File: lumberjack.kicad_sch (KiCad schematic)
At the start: 159 parts, among them J1 USB, J2 AVR_ISP_6, J3 JST, J4 JST, SW1 RESET, SW2 BOOT, U1 ATMEGA328-PU, Y1 16MHz

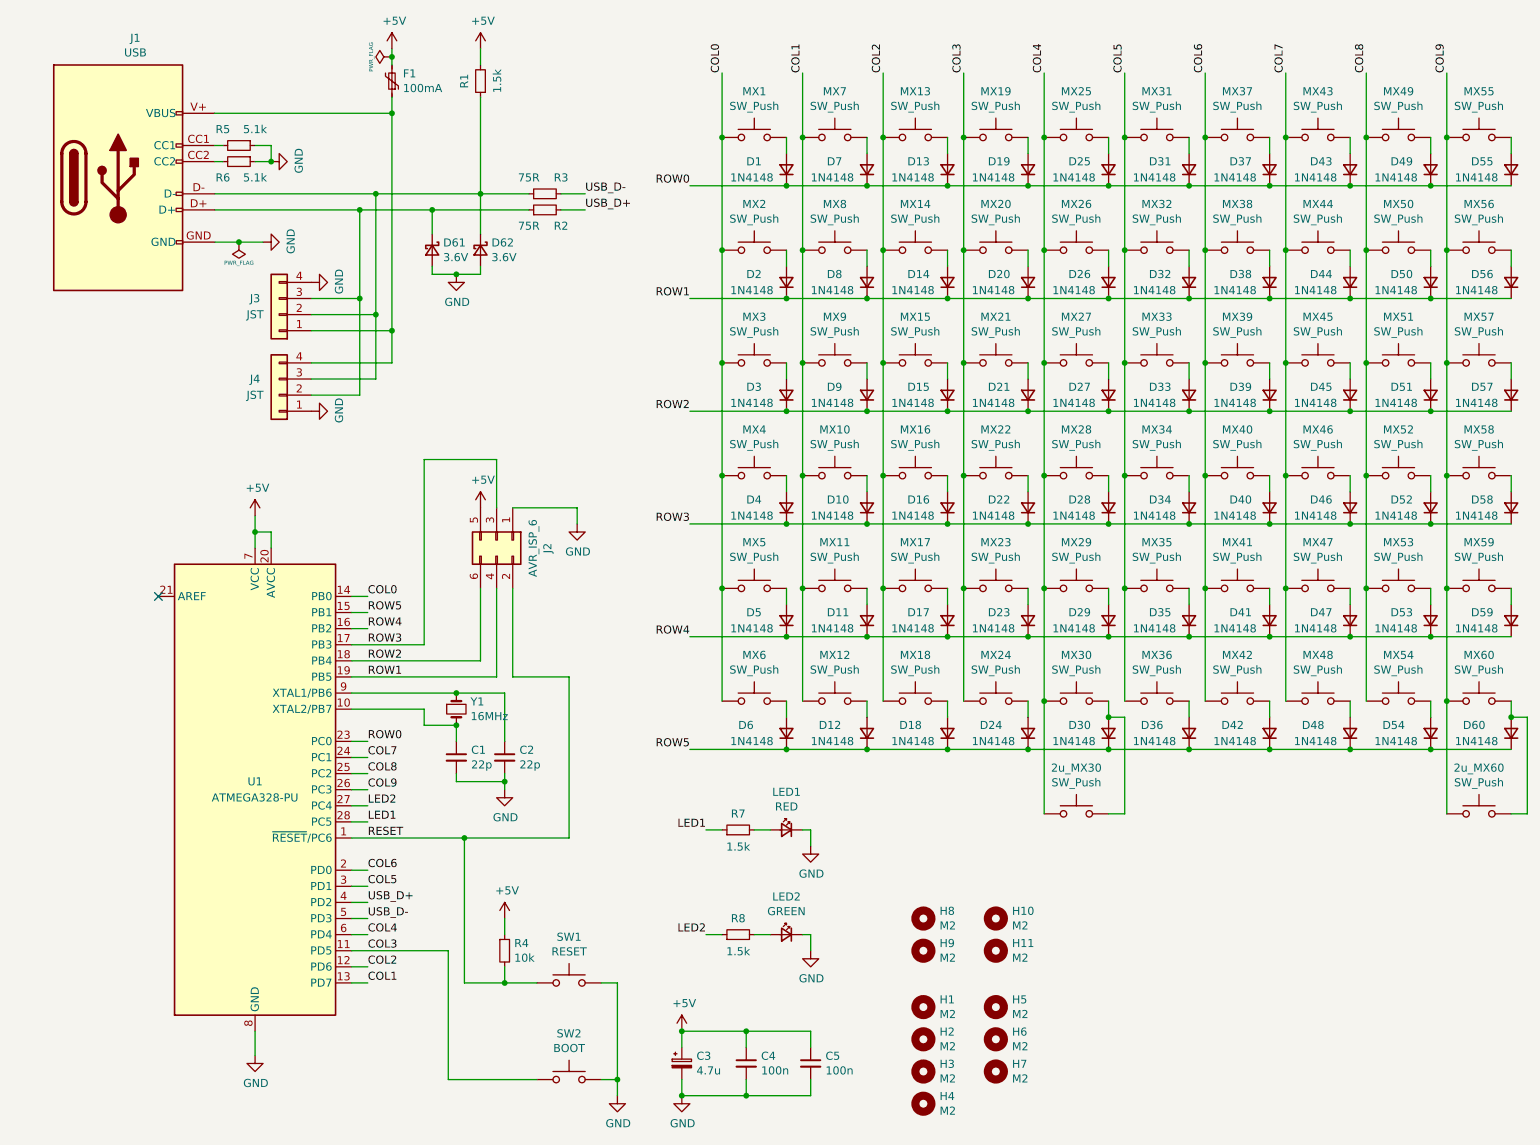
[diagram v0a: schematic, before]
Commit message: feat: change mcu to use pro-micro
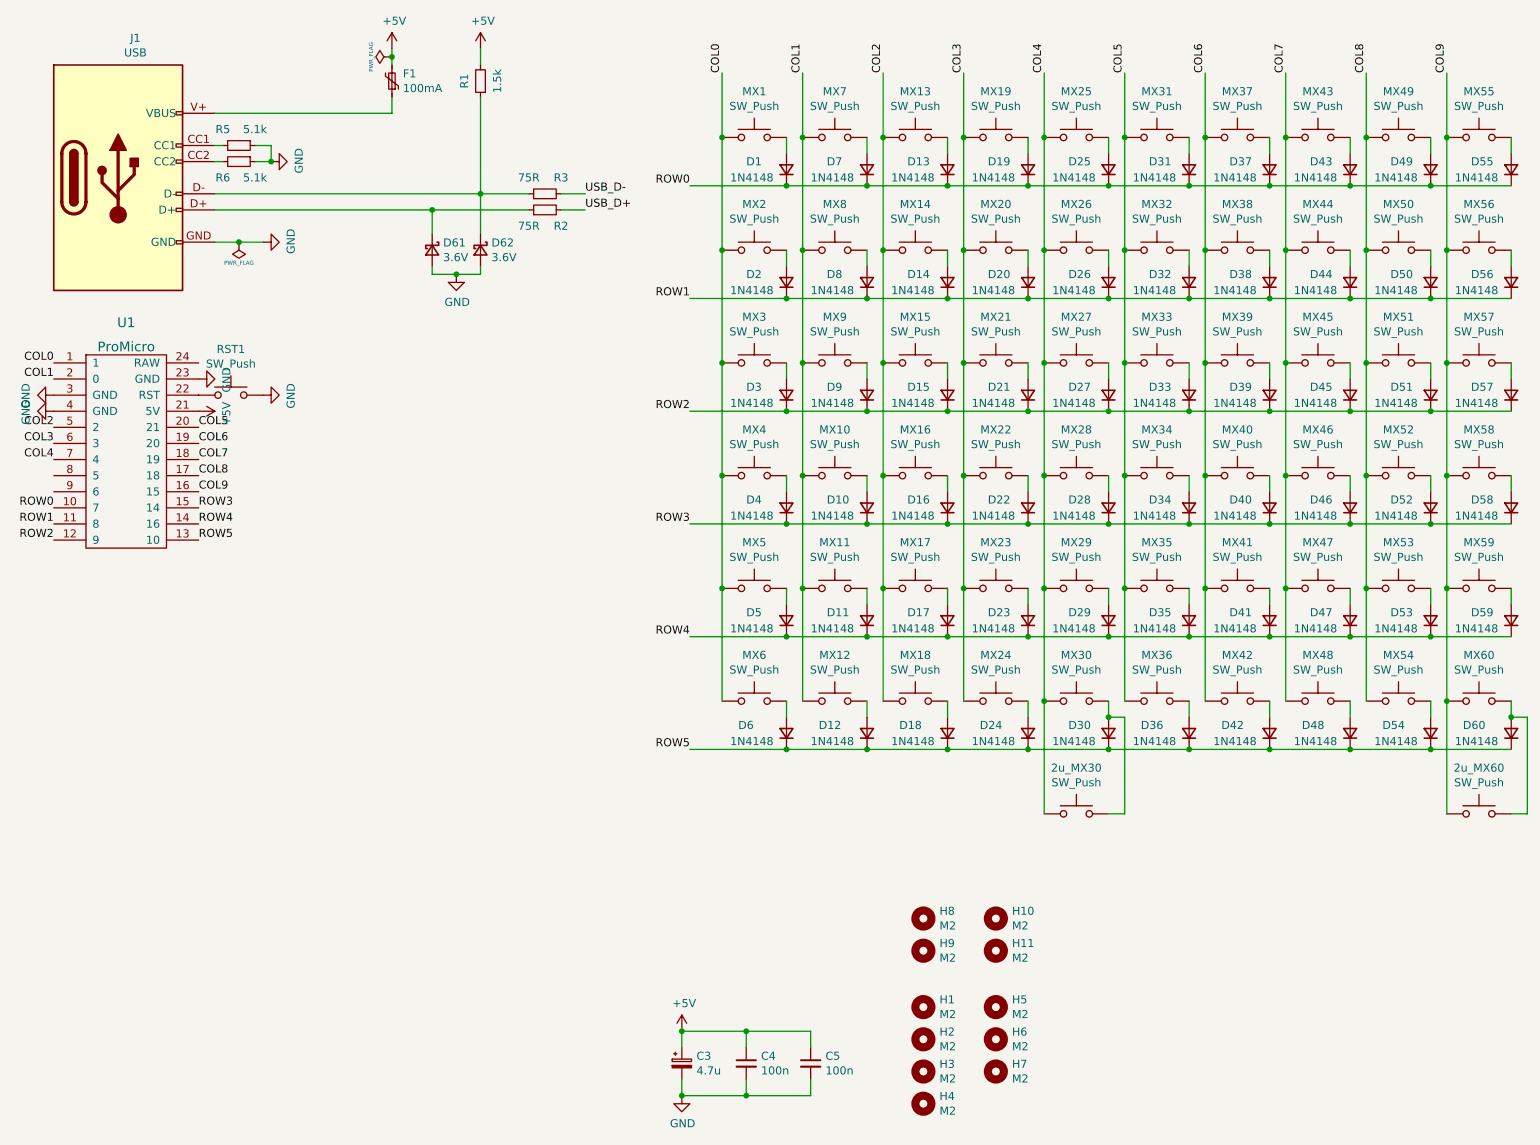
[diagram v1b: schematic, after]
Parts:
- removed C1, C2: 22p, Capacitor_THT:C_Disc_D3.0mm_W1.6mm_P2.50mm, symbol Device:C_Small
- removed J2: AVR_ISP_6, Connector_PinHeader_2.54mm:PinHeader_2x03_P2.54mm_Vertical, symbol Connector_Generic:Conn_02x03_Odd_Even
- removed J3: JST, Connector_JST:JST_SH_SM04B-SRSS-TB_1x04-1MP_P1.00mm_Horizontal, symbol Connector_Generic:Conn_01x04
- removed J4: JST, lumberjack:S4B-ZRLFSN, symbol Connector_Generic:Conn_01x04
- removed LED1: RED, LED_THT:LED_D3.0mm, symbol Device:LED_Small
- removed LED2: GREEN, LED_THT:LED_D3.0mm, symbol Device:LED_Small
- removed R4: 10k, Resistor_THT:R_Axial_DIN0204_L3.6mm_D1.6mm_P7.62mm_Horizontal, symbol Device:R_Small
- removed R7, R8: 1.5k, Resistor_THT:R_Axial_DIN0204_L3.6mm_D1.6mm_P7.62mm_Horizontal, symbol Device:R_Small
- removed SW1: RESET, Button_Switch_THT:SW_PUSH_6mm, symbol Switch:SW_Push
- removed SW2: BOOT, Button_Switch_THT:SW_PUSH_6mm, symbol Switch:SW_Push
- removed U1: ATMEGA328-PU, Package_DIP:DIP-28_W7.62mm, symbol MCU_Microchip_ATmega:ATmega328P-P
- removed Y1: 16MHz, Crystal:Crystal_HC49-4H_Vertical, symbol Device:Crystal_Small
- added RST1: SW_Push, lumberjack:MX_Alps_Choc, symbol Switch:SW_Push
- added U1: ProMicro, lumberjack:ProMicro, symbol contra:ProMicro
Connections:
- net +5V: now also U1.21 (5V)
- net COL0: now also U1.1
- net COL1: now also U1.2 (0)
- net COL2: now also U1.5 (2)
- net COL3: now also U1.6 (3)
- net COL4: now also U1.7 (4)
- net COL5: now also U1.20 (21)
- net COL6: now also U1.19 (20)
- net COL7: now also U1.18 (19)
- net COL8: now also U1.17 (18)
- net COL9: now also U1.16 (15)
- net GND: now also RST1.1, U1.23 (GND), U1.3 (GND), U1.4 (GND)
- net ROW0: now also U1.10 (7)
- net ROW1: now also U1.11 (8)
- net ROW2: now also U1.12 (9)
- net ROW3: now also U1.15 (14)
- net ROW4: now also U1.14 (16)
- net ROW5: now also U1.13 (10)
- new net: RST1.2, U1.22 (RST)
- no-connect marks 1 -> 0

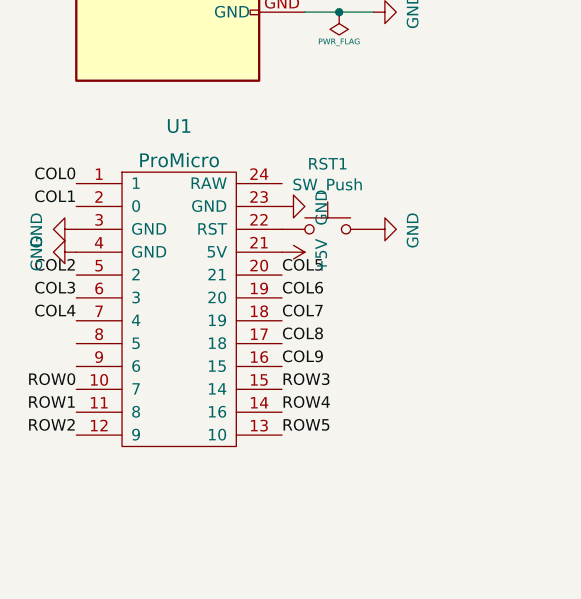
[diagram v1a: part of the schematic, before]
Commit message: fix: update matrix pin assignment
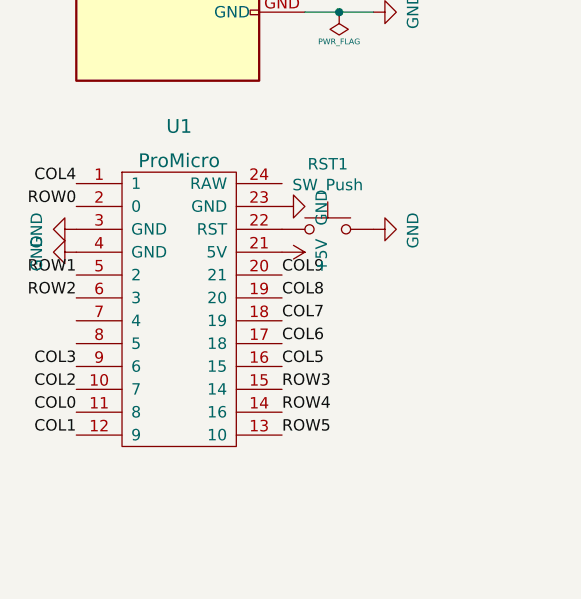
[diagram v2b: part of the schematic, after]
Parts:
- RST1: footprint lumberjack:MX_Alps_Choc -> Molex-0548190589:PushButton_6x6mm_TH
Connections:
- net COL0: now also U1.11 (8); no longer U1.1
- net COL1: now also U1.12 (9); no longer U1.2 (0)
- net COL2: now also U1.10 (7); no longer U1.5 (2)
- net COL3: now also U1.9 (6); no longer U1.6 (3)
- net COL4: now also U1.1; no longer U1.7 (4)
- net COL5: now also U1.16 (15); no longer U1.20 (21)
- net COL6: now also U1.17 (18); no longer U1.19 (20)
- net COL8: now also U1.19 (20); no longer U1.17 (18)
- net COL9: now also U1.20 (21); no longer U1.16 (15)
- net ROW0: now also U1.2 (0); no longer U1.10 (7)
- net ROW1: now also U1.5 (2); no longer U1.11 (8)
- net ROW2: now also U1.6 (3); no longer U1.12 (9)
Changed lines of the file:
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@@
     (effects (font (size 1.27 1.27)) (justify left bottom))
   )
-  (label "COL7" (at 41.91 90.17 0)
+  (label "COL1" (at 19.05 102.87 180)
+    (effects (font (size 1.27 1.27)) (justify right bottom))
+  )
+  (label "COL6" (at 41.91 92.71 0)
     (effects (font (size 1.27 1.27)) (justify left bottom))
   )
@@
     (effects (font (size 1.27 1.27)) (justify right bottom))
   )
-  (label "ROW0" (at 19.05 97.79 180)
-    (effects (font (size 1.27 1.27)) (justify right bottom))
-  )
-  (label "COL8" (at 41.91 92.71 0)
-    (effects (font (size 1.27 1.27)) (justify left bottom))
-  )
-  (label "COL4" (at 19.05 90.17 180)
+  (label "ROW1" (at 19.05 85.09 180)
     (effects (font (size 1.27 1.27)) (justify right bottom))
   )
@@
     (effects (font (size 1.27 1.27)) (justify left bottom))
   )
-  (label "COL5" (at 41.91 85.09 0)
-    (effects (font (size 1.27 1.27)) (justify left bottom))
+  (label "COL4" (at 19.05 74.93 180)
+    (effects (font (size 1.27 1.27)) (justify right bottom))
+  )
+  (label "COL2" (at 19.05 97.79 180)
+    (effects (font (size 1.27 1.27)) (justify right bottom))
   )
   (label "ROW2" (at 119.38 82.55 180)
@@
     (effects (font (size 1.27 1.27)) (justify left bottom))
   )
-  (label "COL9" (at 41.91 95.25 0)
-    (effects (font (size 1.27 1.27)) (justify left bottom))
-  )
   (label "COL2" (at 149.86 29.21 90)
     (effects (font (size 1.27 1.27)) (justify left bottom))
   )
-  (label "ROW5" (at 119.38 135.89 180)
+  (label "COL0" (at 19.05 100.33 180)
     (effects (font (size 1.27 1.27)) (justify right bottom))
   )
-  (label "COL3" (at 19.05 87.63 180)
+  (label "ROW5" (at 119.38 135.89 180)
     (effects (font (size 1.27 1.27)) (justify right bottom))
   )
-  (label "COL6" (at 41.91 87.63 0)
+  (label "COL9" (at 41.91 85.09 0)
     (effects (font (size 1.27 1.27)) (justify left bottom))
   )
-  (label "ROW4" (at 41.91 100.33 0)
+  (label "ROW2" (at 19.05 87.63 180)
+    (effects (font (size 1.27 1.27)) (justify right bottom))
+  )
+  (label "COL8" (at 41.91 87.63 0)
     (effects (font (size 1.27 1.27)) (justify left bottom))
   )
-  (label "COL4" (at 175.26 29.21 90)
+  (label "ROW4" (at 41.91 100.33 0)
     (effects (font (size 1.27 1.27)) (justify left bottom))
   )
-  (label "COL0" (at 19.05 74.93 180)
+  (label "ROW0" (at 19.05 77.47 180)
     (effects (font (size 1.27 1.27)) (justify right bottom))
   )
-  (label "COL2" (at 19.05 85.09 180)
-    (effects (font (size 1.27 1.27)) (justify right bottom))
+  (label "COL5" (at 41.91 95.25 0)
+    (effects (font (size 1.27 1.27)) (justify left bottom))
+  )
+  (label "COL4" (at 175.26 29.21 90)
+    (effects (font (size 1.27 1.27)) (justify left bottom))
   )
   (label "COL1" (at 137.16 29.21 90)
@@
     (effects (font (size 1.27 1.27)) (justify right bottom))
   )
-  (label "ROW2" (at 19.05 102.87 180)
-    (effects (font (size 1.27 1.27)) (justify right bottom))
-  )
-  (label "ROW1" (at 19.05 100.33 180)
-    (effects (font (size 1.27 1.27)) (justify right bottom))
-  )
-  (label "COL1" (at 19.05 77.47 180)
+  (label "COL3" (at 19.05 95.25 180)
     (effects (font (size 1.27 1.27)) (justify right bottom))
   )
@@
     (effects (font (size 1.27 1.27)) (justify right bottom))
   )
+  (label "COL7" (at 41.91 90.17 0)
+    (effects (font (size 1.27 1.27)) (justify left bottom))
+  )
   (label "ROW5" (at 41.91 102.87 0)
     (effects (font (size 1.27 1.27)) (justify left bottom))
@@
     (property "Reference" "RST1" (id 0) (at 46.99 72.771 0))
     (property "Value" "SW_Push" (id 1) (at 46.99 75.0824 0))
-    (property "Footprint" "lumberjack:MX_Alps_Choc" (id 2) (at 46.99 74.93 0)
+    (property "Footprint" "Molex-0548190589:PushButton_6x6mm_TH" (id 2) (at 46.99 74.93 0)
       (effects (font (size 1.27 1.27)) hide)
     )
@@
     )
     (path "/731a7db5-97a7-4f3a-9e89-a36feaaee489"
-      (reference "RST1") (unit 1) (value "SW_Push") (footprint "lumberjack:MX_Alps_Choc")
+      (reference "RST1") (unit 1) (value "SW_Push") (footprint "Molex-0548190589:PushButton_6x6mm_TH")
     )
     (path "/82b2f961-7a58-4751-936a-ca422f92d494"
